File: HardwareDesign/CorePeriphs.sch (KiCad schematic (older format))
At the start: 10 parts, among them J303 Conn_01x05, U301 82C55A, U302 82C54, U303 MC6850

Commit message: more work on preparing for PCB design
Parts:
- added C304, C305, C306, C307, C308: 1μC, symbol device:CP
- added J304: Conn_01x05, symbol Connector_Generic:Conn_01x05
- added J305, J306: Conn_01x09, symbol Connector_Generic:Conn_01x09
- added U304: MAX232CPE, DIP794W47P254L1943H457Q16, symbol MAX232CPE:MAX232CPE
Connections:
- net labels added: Ext_CTS, Ext_RTS, Ext_RxD, Ext_TxD, PA0, PA1, PA2, PA3, PA4, PA5, PA6, PA7, PB0, PB1, PB2, PB3, PB4, PB5, PB6, PB7
- wire segments 146 -> 222
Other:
- note added: "GPIO headers"
- note added: "RS-232 transceiver"
- note added: "TODO: this section is not correct currently"
- note added: "To external RS-232"
- note added: "decoupling caps (place\nnear U301-U303)"
- moved on the sheet: C301, C302, C303

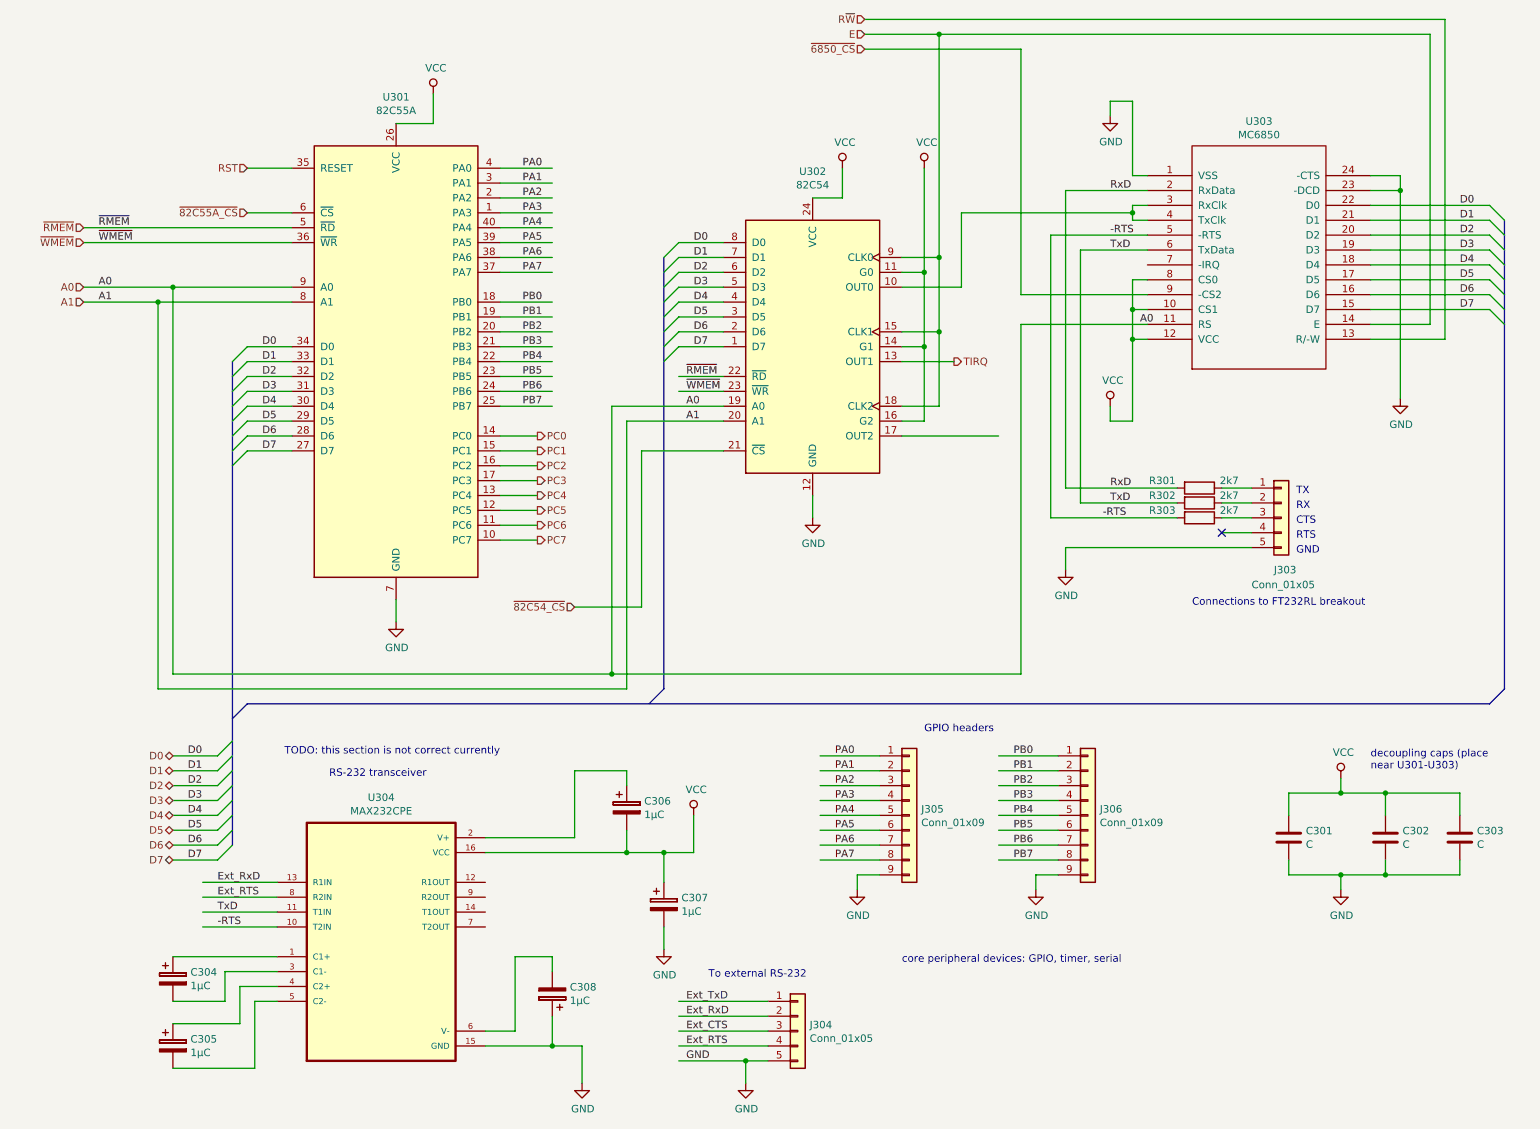
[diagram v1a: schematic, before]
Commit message: correct connections for RS-232?
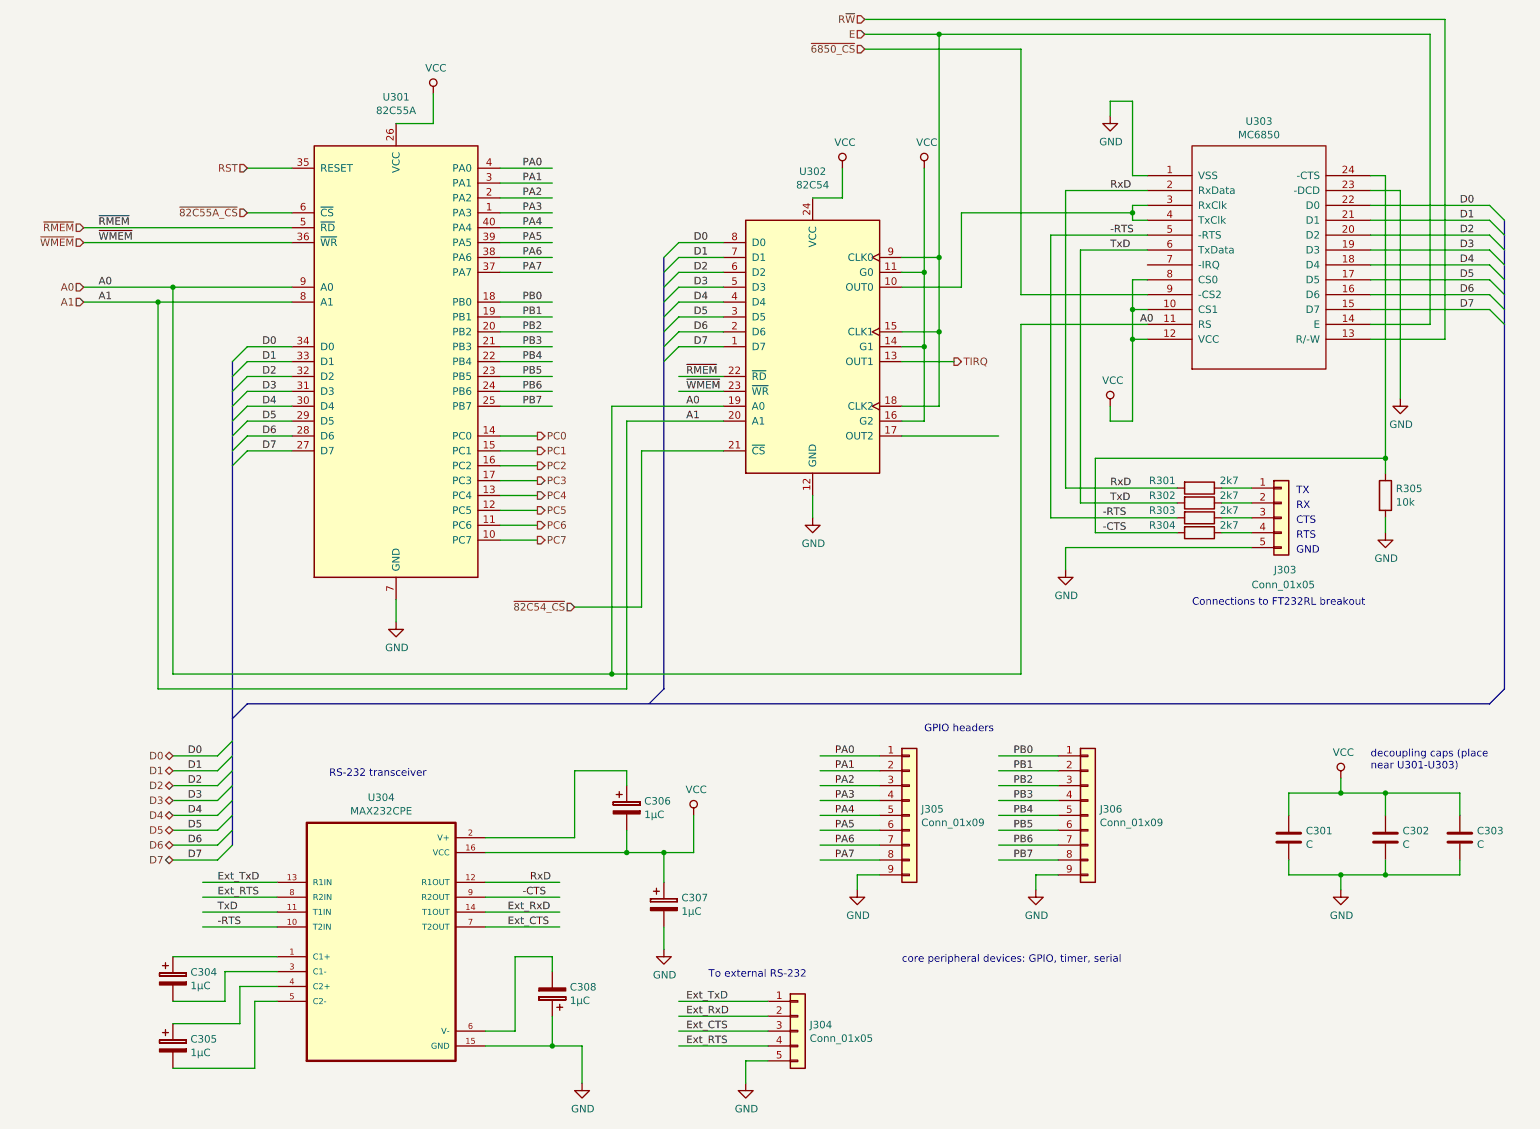
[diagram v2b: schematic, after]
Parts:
- added R304: 2k7, symbol device:R
- added R305: 10k, symbol device:R
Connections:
- net labels added: -CTS
- wire segments 222 -> 230
- no-connect marks 1 -> 0
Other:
- note removed: "TODO: this section is not correct currently"
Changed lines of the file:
@@
 	7350 2050 7350 3950
-Wire Wire Line
-	9500 1650 9700 1650
 Wire Wire Line
 	7450 4150 7450 4300
@@
 Wire Wire Line
 	9500 2550 10300 2550
-Wire Wire Line
-	9700 1650 9700 1750
 $Comp
 L power:GND #PWR?
@@
 Wire Wire Line
 	9500 1750 9700 1750
-Connection ~ 9700 1750
 Wire Wire Line
 	9700 1750 9700 3150
-Wire Wire Line
-	8700 4050 8500 4050
-NoConn ~ 8500 4050
 Wire Wire Line
 	7900 1850 7900 1900
@@
 	2150 6500 1650 6500
 Text Label 1750 6400 0    50   ~ 0
-Ext_RxD
+Ext_TxD
 Text Label 1750 6500 0    50   ~ 0
 Ext_RTS
@@
 Text Label 4900 7500 0    50   ~ 0
 Ext_RTS
-Text Label 4900 7600 0    50   ~ 0
-GND
 $Comp
 L power:GND #PWR?
@@
 Wire Wire Line
 	5300 7750 5300 7600
-Connection ~ 5300 7600
-Wire Wire Line
-	5300 7600 4850 7600
-Text Notes 2200 5550 0    50   ~ 0
-TODO: this section is not correct currently
 $Comp
 L Connector_Generic:Conn_01x09 J305
@@
 Wire Wire Line
 	7250 6350 7250 6450
+Wire Wire Line
+	9500 1650 9600 1650
+Wire Wire Line
+	9600 1650 9600 3550
+Wire Wire Line
+	7650 3550 7650 4050
+Text Label 7700 4050 0    50   ~ 0
+-CTS
+$Comp
+L device:R R305
+U 1 1 61113D93
+P 9600 3800
+F 0 "R305" H 9670 3846 50  0000 L CNN
+F 1 "10k" H 9670 3755 50  0000 L CNN
+F 2 "" V 9530 3800 50  0001 C CNN
+F 3 "" H 9600 3800 50  0001 C CNN
+	1    9600 3800
+	1    0    0    -1
+$EndComp
+Wire Wire Line
+	9600 3650 9600 3550
+Connection ~ 9600 3550
+Wire Wire Line
+	9600 3950 9600 4050
+$Comp
+L power:GND #PWR?
+U 1 1 61136F82
+P 9600 4050
+F 0 "#PWR?" H 9600 3800 50  0001 C CNN
+F 1 "GND" H 9605 3877 50  0000 C CNN
+F 2 "" H 9600 4050 50  0001 C CNN
+F 3 "" H 9600 4050 50  0001 C CNN
+	1    9600 4050
+	1    0    0    -1
+$EndComp
+Wire Wire Line
+	7650 3550 9600 3550
+$Comp
+L device:R R304
+U 1 1 6114E6B2
+P 8350 4050
+F 0 "R304" V 8300 3800 50  0000 C CNN
+F 1 "2k7" V 8300 4250 50  0000 C CNN
+F 2 "" V 8280 4050 50  0001 C CNN
+F 3 "" H 8350 4050 50  0001 C CNN
+	1    8350 4050
+	0    1    1    0
+$EndComp
+Wire Wire Line
+	8500 4050 8700 4050
+Wire Wire Line
+	8200 4050 7650 4050
+Wire Wire Line
+	4050 6600 3550 6600
+Wire Wire Line
+	4050 6700 3550 6700
+Wire Wire Line
+	4050 6400 3550 6400
+Wire Wire Line
+	4050 6500 3550 6500
 Wire Bus Line
 	1950 5200 10300 5200
@@
 Wire Bus Line
 	1850 2900 1850 6150
+Text Label 3850 6400 0    50   ~ 0
+RxD
+Text Label 3800 6500 0    50   ~ 0
+-CTS
+Text Label 3700 6600 0    50   ~ 0
+Ext_RxD
+Text Label 3700 6700 0    50   ~ 0
+Ext_CTS
 $EndSCHEMATC

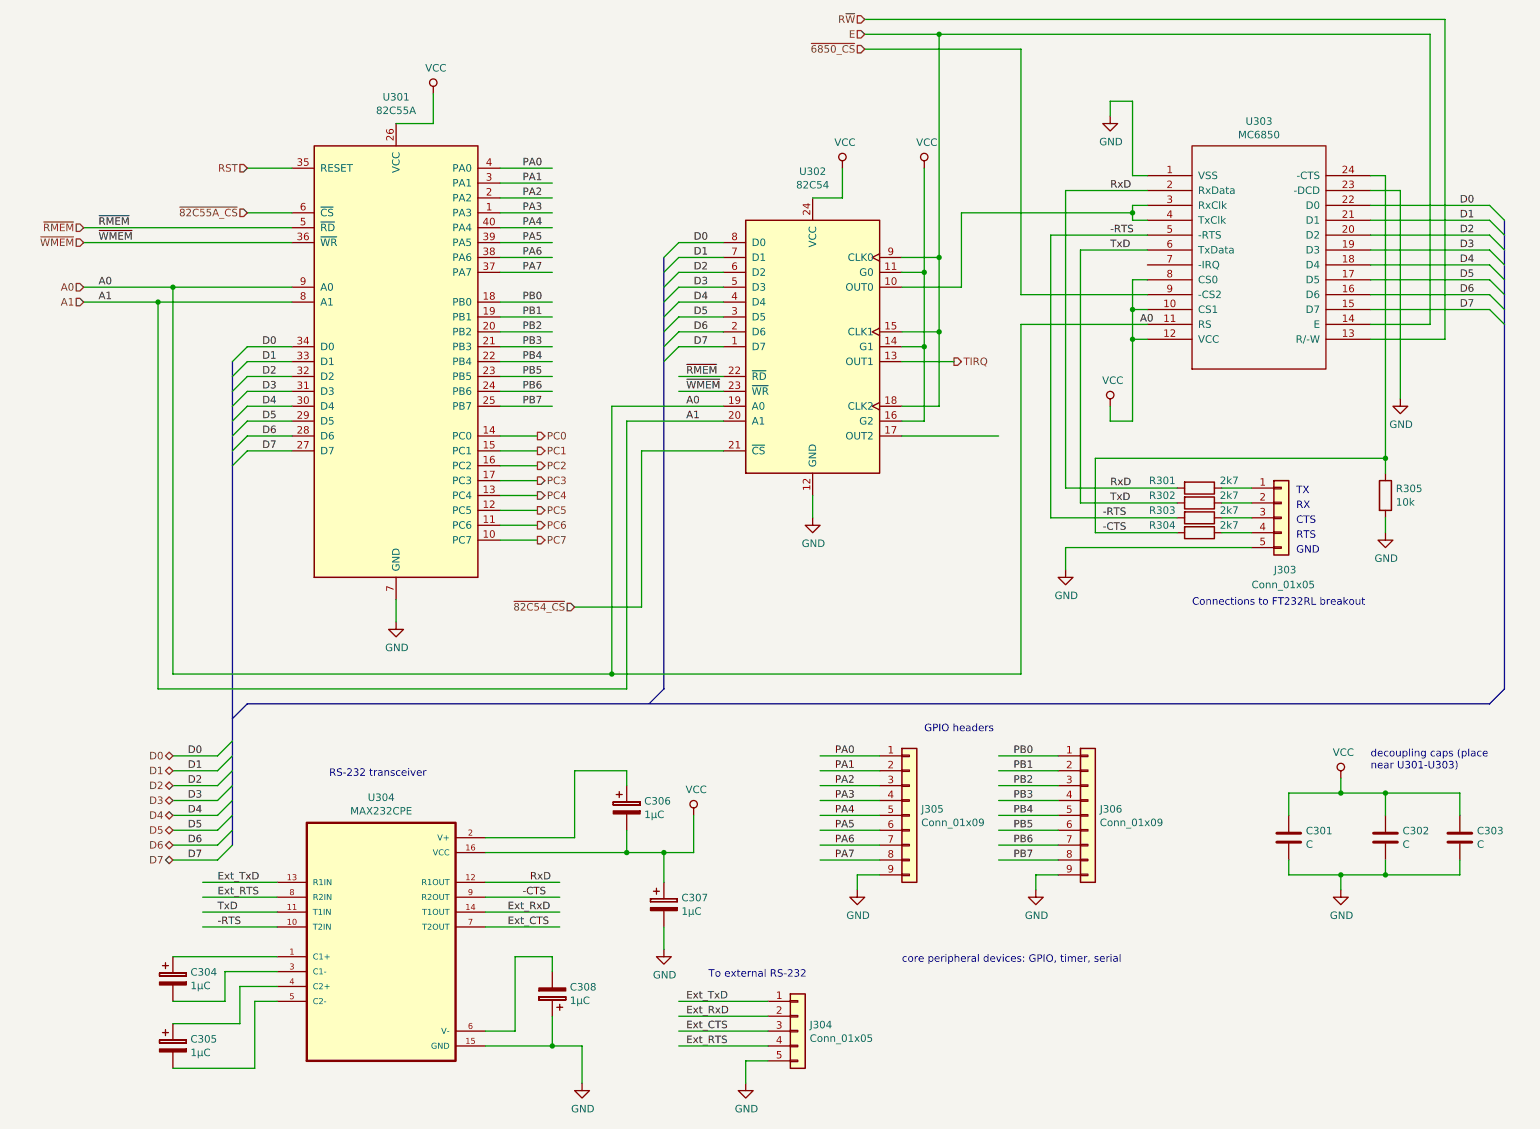
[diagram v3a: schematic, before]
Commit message: a few more consistency tweaks before PCB layout
Routed second timer/counter output to backplane connector,
just in case we want to use it for something eventually
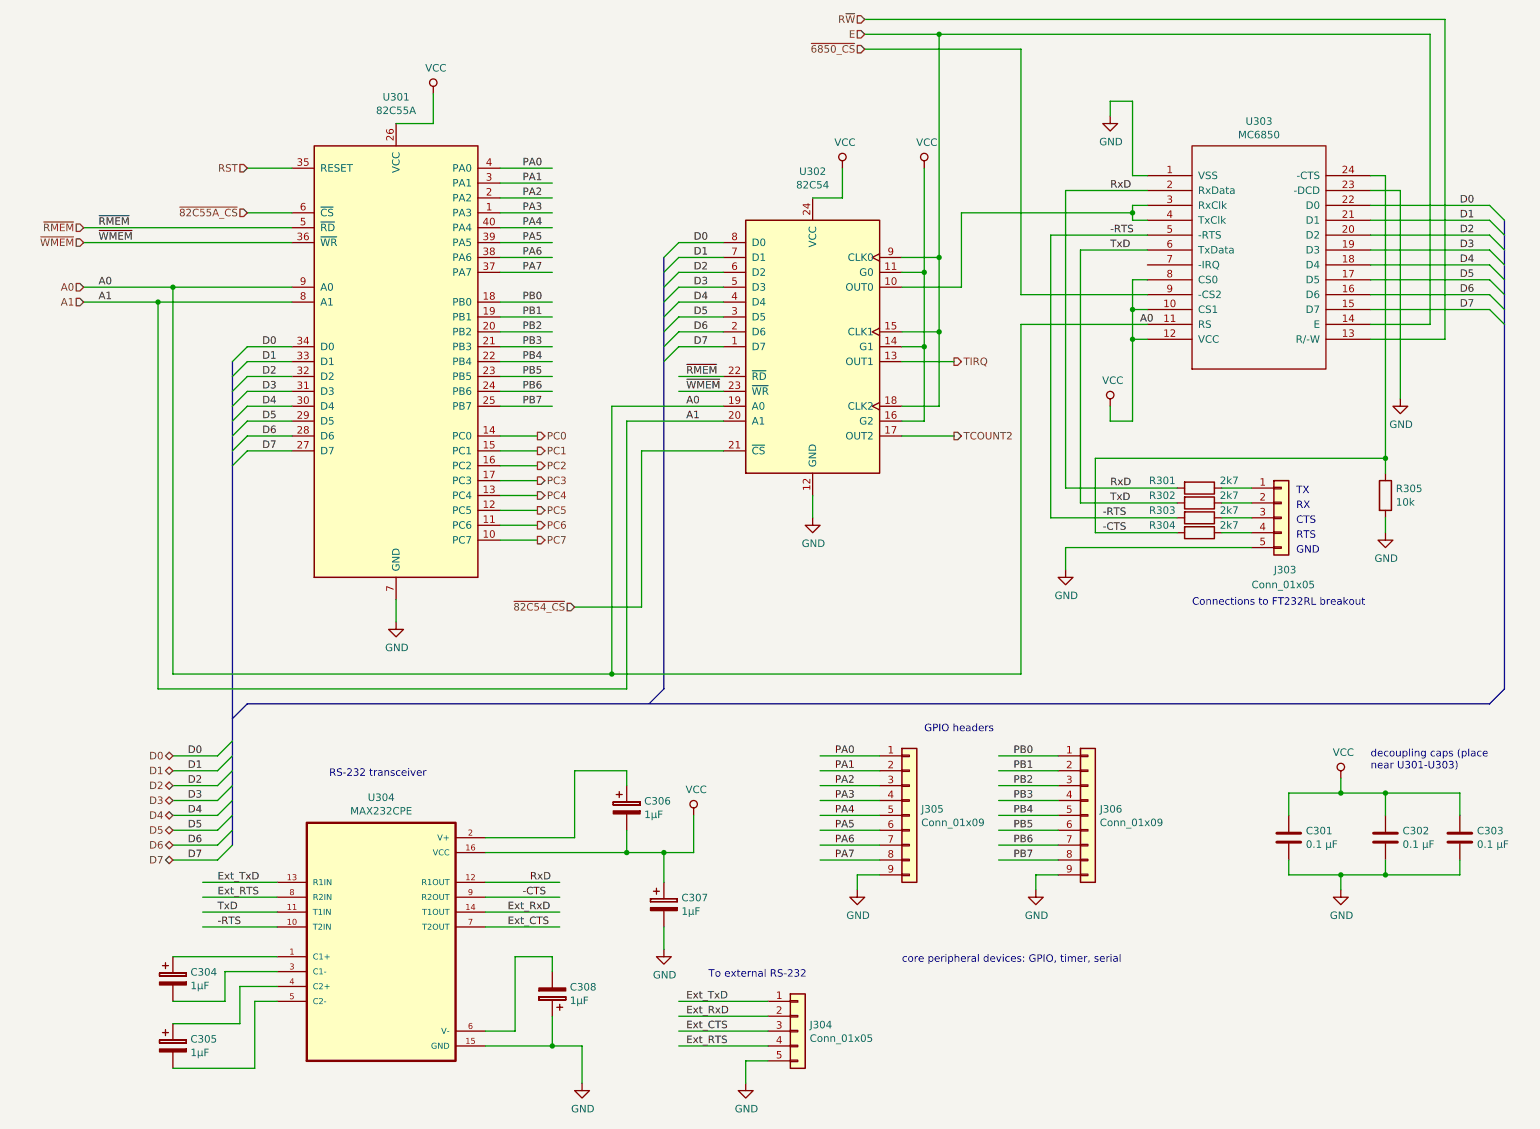
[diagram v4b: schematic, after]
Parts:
- C301, C302, C303: value C -> 0.1 μF
- C304, C305, C306, C307, C308: value 1μC -> 1μF
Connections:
- net labels added: TCOUNT2
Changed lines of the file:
@@
 P 8950 6100
 F 0 "C301" H 9065 6146 50  0000 L CNN
-F 1 "C" H 9065 6055 50  0000 L CNN
+F 1 "0.1 μF" H 9065 6055 50  0000 L CNN
 F 2 "" H 8988 5950 50  0001 C CNN
 F 3 "" H 8950 6100 50  0001 C CNN
@@
 P 9600 6100
 F 0 "C302" H 9715 6146 50  0000 L CNN
-F 1 "C" H 9715 6055 50  0000 L CNN
+F 1 "0.1 μF" H 9715 6055 50  0000 L CNN
 F 2 "" H 9638 5950 50  0001 C CNN
 F 3 "" H 9600 6100 50  0001 C CNN
@@
 	6350 2900 6700 2900
 Wire Wire Line
-	6350 3400 7000 3400
+	6350 3400 6700 3400
 $Comp
 L MC6850:MC6850 U303
@@
 P 10100 6100
 F 0 "C303" H 10215 6146 50  0000 L CNN
-F 1 "C" H 10215 6055 50  0000 L CNN
+F 1 "0.1 μF" H 10215 6055 50  0000 L CNN
 F 2 "" H 10138 5950 50  0001 C CNN
 F 3 "" H 10100 6100 50  0001 C CNN
@@
 P 1450 7050
 F 0 "C304" H 1568 7096 50  0000 L CNN
-F 1 "1μC" H 1568 7005 50  0000 L CNN
+F 1 "1μF" H 1568 7005 50  0000 L CNN
 F 2 "" H 1488 6900 50  0001 C CNN
 F 3 "" H 1450 7050 50  0001 C CNN
@@
 P 1450 7500
 F 0 "C305" H 1568 7546 50  0000 L CNN
-F 1 "1μC" H 1568 7455 50  0000 L CNN
+F 1 "1μF" H 1568 7455 50  0000 L CNN
 F 2 "" H 1488 7350 50  0001 C CNN
 F 3 "" H 1450 7500 50  0001 C CNN
@@
 P 4500 5900
 F 0 "C306" H 4618 5946 50  0000 L CNN
-F 1 "1μC" H 4618 5855 50  0000 L CNN
+F 1 "1μF" H 4618 5855 50  0000 L CNN
 F 2 "" H 4538 5750 50  0001 C CNN
 F 3 "" H 4500 5900 50  0001 C CNN
@@
 P 4750 6550
 F 0 "C307" H 4868 6596 50  0000 L CNN
-F 1 "1μC" H 4868 6505 50  0000 L CNN
+F 1 "1μF" H 4868 6505 50  0000 L CNN
 F 2 "" H 4788 6400 50  0001 C CNN
 F 3 "" H 4750 6550 50  0001 C CNN
@@
 P 4000 7150
 F 0 "C308" H 3882 7104 50  0000 R CNN
-F 1 "1μC" H 3882 7195 50  0000 R CNN
+F 1 "1μF" H 3882 7195 50  0000 R CNN
 F 2 "" H 4038 7000 50  0001 C CNN
 F 3 "" H 4000 7150 50  0001 C CNN
@@
 Text Label 3700 6700 0    50   ~ 0
 Ext_CTS
+Text HLabel 6700 3400 2    50   Output ~ 0
+TCOUNT2
 Wire Bus Line
 	1950 5200 10300 5200

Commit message: assigned component footprints
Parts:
- C301, C302, C303: footprint (none) -> Capacitor_THT:C_Disc_D5.0mm_W2.5mm_P2.50mm
- C304, C305, C306, C307, C308: footprint (none) -> Capacitor_THT:CP_Radial_Tantal_D5.0mm_P5.00mm
- J303, J304: footprint (none) -> Connector_PinHeader_2.54mm:PinHeader_1x05_P2.54mm_Vertical
- J305, J306: footprint (none) -> Connector_PinHeader_2.54mm:PinHeader_1x09_P2.54mm_Vertical
- R301, R302, R303, R304, R305: footprint (none) -> Resistor_THT:R_Axial_DIN0204_L3.6mm_D1.6mm_P7.62mm_Horizontal
- U301: footprint Package_DIP:DIP-40_W15.24mm -> Package_DIP:DIP-40_W15.24mm_Socket
- U302: footprint Housings_DIP:DIP-24_W15.24mm -> Package_DIP:DIP-24_W15.24mm_Socket
- U303: footprint MODULE -> Package_DIP:DIP-24_W15.24mm_Socket
- U304: footprint DIP794W47P254L1943H457Q16 -> Package_DIP:DIP-16_W7.62mm_Socket
